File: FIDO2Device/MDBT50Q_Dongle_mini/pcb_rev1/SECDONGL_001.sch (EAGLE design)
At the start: 35 parts, among them CN1 CX60-24S-UNIT, CN2 IF_4PIN, CN3 IF_2PIN_SOL, CN4 IF_2PIN_SOL, SW1 SKRPACE010, SW2 SKTADAE010, U1 MDBT50Q-P1M, U2 MIC5323-3.3YMT-TR, X1 NX3215SA-32.768K-STD-MUA-9

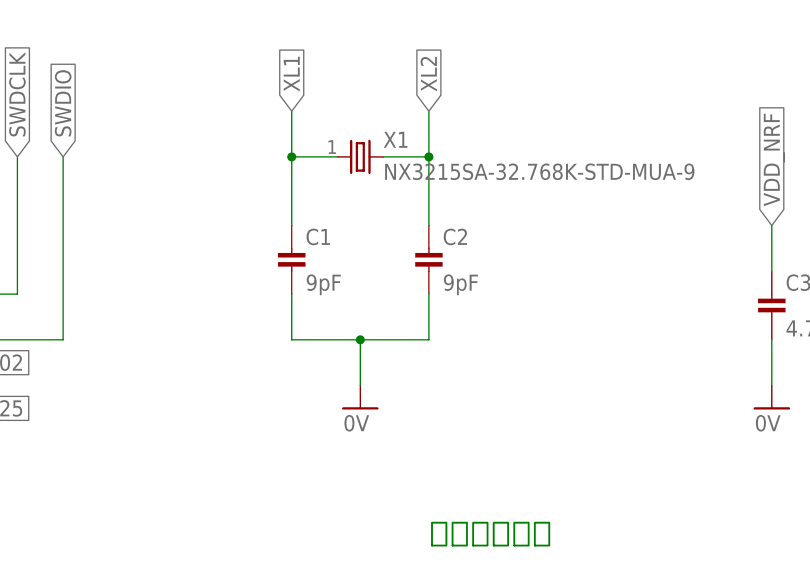
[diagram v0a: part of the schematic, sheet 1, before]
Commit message: 回路図を修正
・定数を実際の使用部品と整合
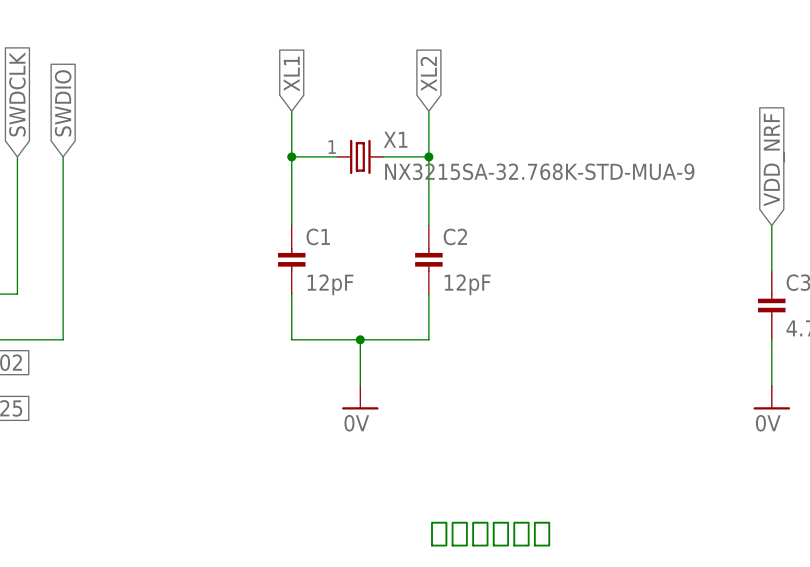
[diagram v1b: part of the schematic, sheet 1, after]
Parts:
- C1, C2: value 9pF -> 12pF
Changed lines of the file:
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@@
 <part name="FRAME1" library="Generic" deviceset="A4L-LOC" device=""/>
 <part name="X1" library="Parts" deviceset="NX3215SA" device="-32.768K-STD-MUA-9" value="NX3215SA-32.768K-STD-MUA-9"/>
-<part name="C1" library="Parts" deviceset="CAP" device="_0603" value="9pF"/>
-<part name="C2" library="Parts" deviceset="CAP" device="_0603" value="9pF"/>
+<part name="C1" library="Parts" deviceset="CAP" device="_0603" value="12pF"/>
+<part name="C2" library="Parts" deviceset="CAP" device="_0603" value="12pF"/>
 <part name="GND1" library="Supply" deviceset="0V" device=""/>
 <part name="C3" library="Parts" deviceset="CAP" device="_0603" value="4.7uF"/>
